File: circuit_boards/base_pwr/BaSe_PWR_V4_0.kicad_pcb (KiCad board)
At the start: 2 copper layers, 15 parts, among them J1 USB_B, J2 MOTOR, J3 MEAS, J5 Conn_02x19_Odd_Even, U1 DRV8220, U2 STM32F070CBTx

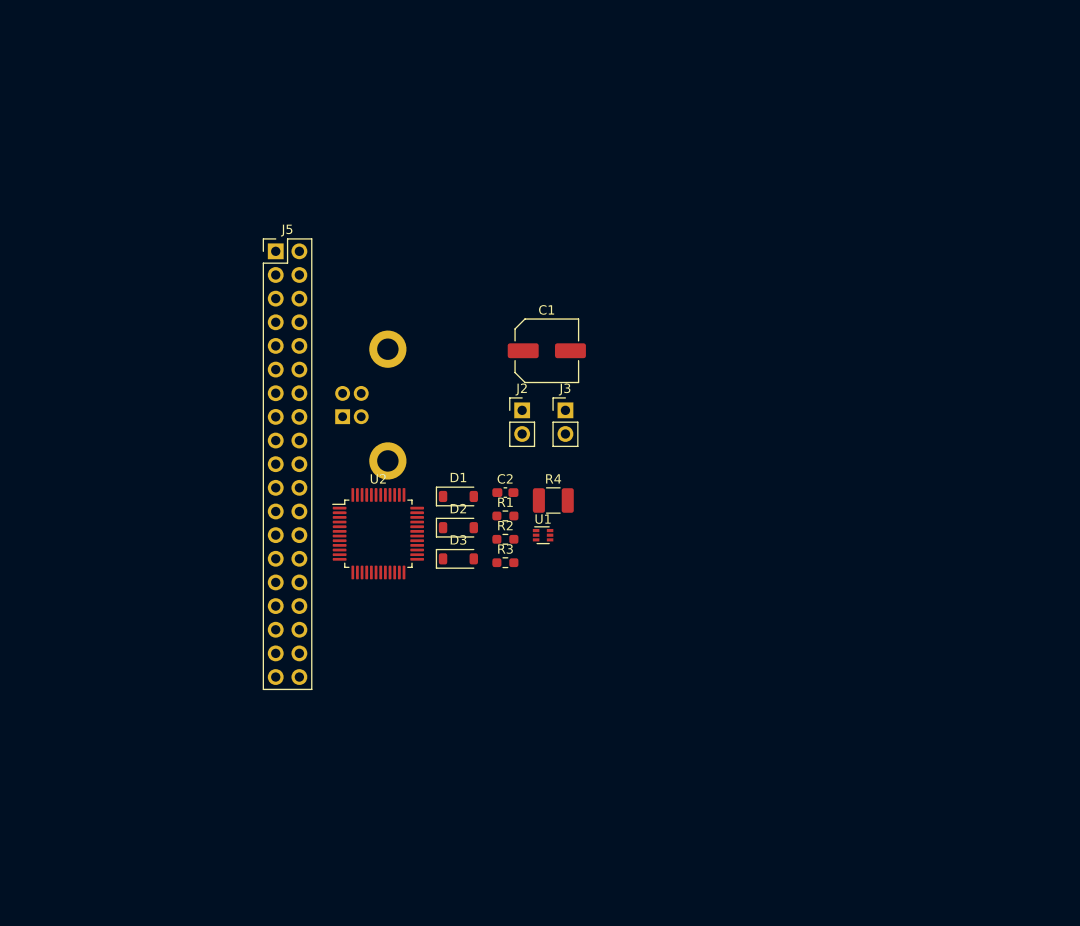
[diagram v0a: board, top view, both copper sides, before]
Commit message: base_pwr: rescure schematic parts from old version (v3.2) and start with mcu wiring
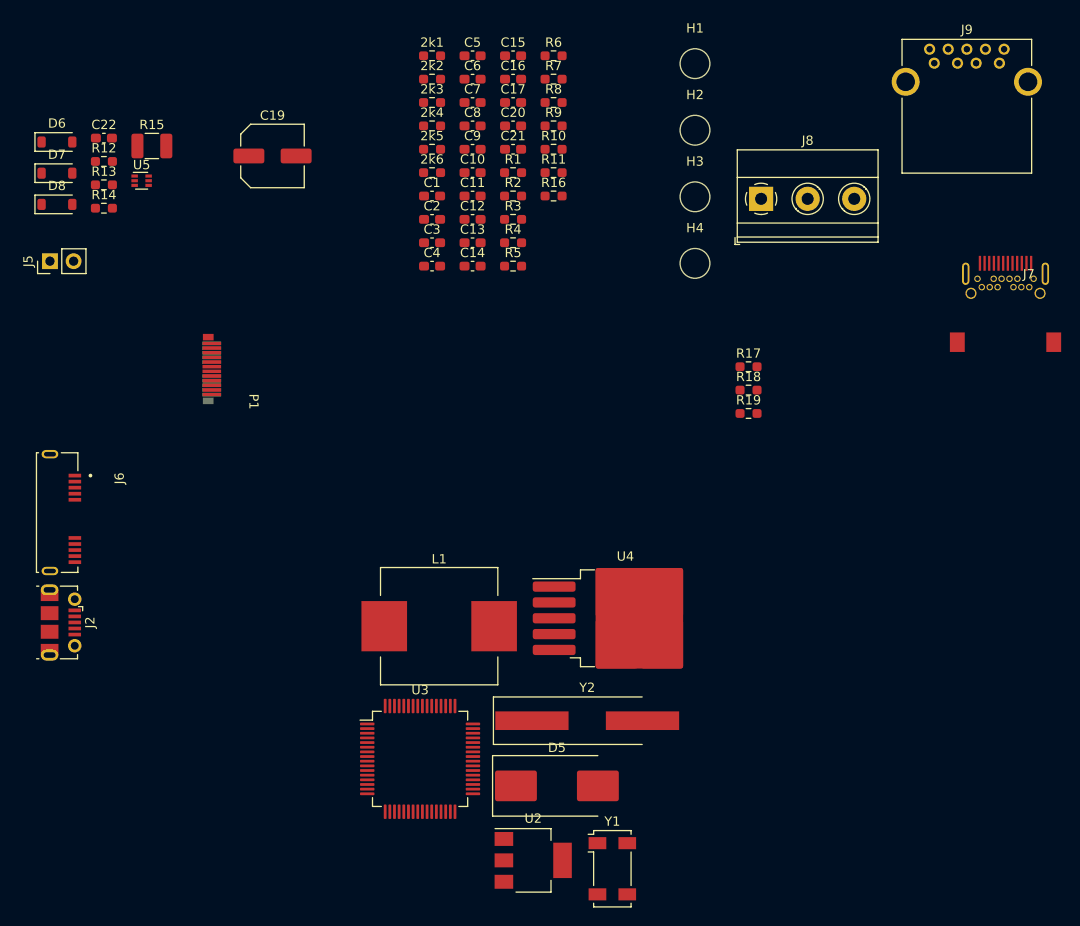
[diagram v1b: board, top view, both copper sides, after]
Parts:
- removed J1: USB_B, Connector_USB:USB_B_Lumberg_2411_02_Horizontal
- removed J3: MEAS, Connector_PinHeader_2.54mm:PinHeader_1x02_P2.54mm_Vertical
- removed the J5 at (79.2, 43.9)
- added 2k1: ~, Resistor_SMD:R_0603_1608Metric_Pad0.98x0.95mm_HandSolder, F.Cu at (96.0, 22.9)
- added 2k2: ~, Resistor_SMD:R_0603_1608Metric_Pad0.98x0.95mm_HandSolder, F.Cu at (96.0, 25.4)
- added 2k3: ~, Resistor_SMD:R_0603_1608Metric_Pad0.98x0.95mm_HandSolder, F.Cu at (96.0, 28.0)
- added 2k4: ~, Resistor_SMD:R_0603_1608Metric_Pad0.98x0.95mm_HandSolder, F.Cu at (96.0, 30.5)
- added 2k5: ~, Resistor_SMD:R_0603_1608Metric_Pad0.98x0.95mm_HandSolder, F.Cu at (96.0, 33.0)
- added 2k6: ~, Resistor_SMD:R_0603_1608Metric_Pad0.98x0.95mm_HandSolder, F.Cu at (96.0, 35.5)
- added C1: ~, Capacitor_SMD:C_0603_1608Metric_Pad1.08x0.95mm_HandSolder, F.Cu at (96.0, 38.0)
- added C10: C, Capacitor_SMD:C_0603_1608Metric_Pad1.08x0.95mm_HandSolder, F.Cu at (100.4, 35.5)
- added C11: 100nF, Capacitor_SMD:C_0603_1608Metric_Pad1.08x0.95mm_HandSolder, F.Cu at (100.4, 38.0)
- added C12: 100nF, Capacitor_SMD:C_0603_1608Metric_Pad1.08x0.95mm_HandSolder, F.Cu at (100.4, 40.5)
- added C13: 100nF, Capacitor_SMD:C_0603_1608Metric_Pad1.08x0.95mm_HandSolder, F.Cu at (100.4, 43.0)
- added C14: ~, Capacitor_SMD:C_0603_1608Metric_Pad1.08x0.95mm_HandSolder, F.Cu at (100.4, 45.5)
- added C15: 100nF, Capacitor_SMD:C_0603_1608Metric_Pad1.08x0.95mm_HandSolder, F.Cu at (104.7, 22.9)
- added C16: 100nF, Capacitor_SMD:C_0603_1608Metric_Pad1.08x0.95mm_HandSolder, F.Cu at (104.7, 25.4)
- added C17: ~, Capacitor_SMD:C_0603_1608Metric_Pad1.08x0.95mm_HandSolder, F.Cu at (104.7, 28.0)
- added C2: ~, Capacitor_SMD:C_0603_1608Metric_Pad1.08x0.95mm_HandSolder, F.Cu at (96.0, 40.5)
- added C20: ~, Capacitor_SMD:C_0603_1608Metric_Pad1.08x0.95mm_HandSolder, F.Cu at (104.7, 30.5)
- added C21: ~, Capacitor_SMD:C_0603_1608Metric_Pad1.08x0.95mm_HandSolder, F.Cu at (104.7, 33.0)
- added C3: ~, Capacitor_SMD:C_0603_1608Metric_Pad1.08x0.95mm_HandSolder, F.Cu at (96.0, 43.0)
- added C4: ~, Capacitor_SMD:C_0603_1608Metric_Pad1.08x0.95mm_HandSolder, F.Cu at (96.0, 45.5)
- added C5: 20pF, Capacitor_SMD:C_0603_1608Metric_Pad1.08x0.95mm_HandSolder, F.Cu at (100.4, 22.9)
- added C6: 20pF, Capacitor_SMD:C_0603_1608Metric_Pad1.08x0.95mm_HandSolder, F.Cu at (100.4, 25.4)
- added C7: 4.3pF, Capacitor_SMD:C_0603_1608Metric_Pad1.08x0.95mm_HandSolder, F.Cu at (100.4, 28.0)
- added C8: 4.3pF, Capacitor_SMD:C_0603_1608Metric_Pad1.08x0.95mm_HandSolder, F.Cu at (100.4, 30.5)
- added C9: 100nF, Capacitor_SMD:C_0603_1608Metric_Pad1.08x0.95mm_HandSolder, F.Cu at (100.4, 33.0)
- added D5: SK34-TP, Diode_SMD:D_SMC_Handsoldering, F.Cu at (109.4, 101.3)
- added H1: MountingHole, MountingHole:MountingHole_3.2mm_M3_DIN965, F.Cu at (124.3, 23.8)
- added H2: MountingHole, MountingHole:MountingHole_3.2mm_M3_DIN965, F.Cu at (124.3, 30.9)
- added H3: MountingHole, MountingHole:MountingHole_3.2mm_M3_DIN965, F.Cu at (124.3, 38.1)
- added H4: MountingHole, MountingHole:MountingHole_3.2mm_M3_DIN965, F.Cu at (124.3, 45.2)
- added J2: USB_B_Micro, Connector_USB:USB_Micro-B_Molex-105017-0001, F.Cu at (56.2, 83.8)
- added J6: USB3_B_Micro, g7_connectors:conn_usb3bmicro_GSB343K331HR, F.Cu at (55.0, 72.0)
- added J7: USB_C_Receptacle, g7_connectors:conn_usbc_socket_RAHPCUC31AU1TR, F.Cu at (157.6, 46.9)
- added J8: Screw_Terminal_01x03, TerminalBlock_Phoenix:TerminalBlock_Phoenix_MKDS-1,5-3_1x03_P5.00mm_Horizontal, F.Cu at (131.4, 38.3)
- added J9: USB3_A, g7_connectors:STEWARD_USB3_A_SS-52000-001, F.Cu at (153.5, 22.2)
- added L1: 47µH, Inductor_SMD:L_Wuerth_WE-PD-Typ-LS_Handsoldering, F.Cu at (96.8, 84.2)
- added P1: USB_C_Plug, g7_connectors:Molex_USBC_Plug_1054440011, F.Cu at (72.9, 56.6)
- added R1: ~, Resistor_SMD:R_0603_1608Metric_Pad0.98x0.95mm_HandSolder, F.Cu at (104.7, 35.5)
- added R10: R, Resistor_SMD:R_0603_1608Metric_Pad0.98x0.95mm_HandSolder, F.Cu at (109.1, 33.0)
- added R11: ~, Resistor_SMD:R_0603_1608Metric_Pad0.98x0.95mm_HandSolder, F.Cu at (109.1, 35.5)
- added R16: R, Resistor_SMD:R_0603_1608Metric_Pad0.98x0.95mm_HandSolder, F.Cu at (109.1, 38.0)
- added R17: 31k6, Resistor_SMD:R_0603_1608Metric_Pad0.98x0.95mm_HandSolder, F.Cu at (130.0, 56.3)
- added R18: 10k, Resistor_SMD:R_0603_1608Metric_Pad0.98x0.95mm_HandSolder, F.Cu at (130.0, 58.8)
- added R19: 38k3, Resistor_SMD:R_0603_1608Metric_Pad0.98x0.95mm_HandSolder, F.Cu at (130.0, 61.4)
- added R2: ~, Resistor_SMD:R_0603_1608Metric_Pad0.98x0.95mm_HandSolder, F.Cu at (104.7, 38.0)
- added R3: R, Resistor_SMD:R_0603_1608Metric_Pad0.98x0.95mm_HandSolder, F.Cu at (104.7, 40.5)
- added R4: R, Resistor_SMD:R_0603_1608Metric_Pad0.98x0.95mm_HandSolder, F.Cu at (104.7, 43.0)
- added R5: 100k, Resistor_SMD:R_0603_1608Metric_Pad0.98x0.95mm_HandSolder, F.Cu at (104.7, 45.5)
- added R6: 33k, Resistor_SMD:R_0603_1608Metric_Pad0.98x0.95mm_HandSolder, F.Cu at (109.1, 22.9)
- added R7: 10k, Resistor_SMD:R_0603_1608Metric_Pad0.98x0.95mm_HandSolder, F.Cu at (109.1, 25.4)
- added R8: 10k, Resistor_SMD:R_0603_1608Metric_Pad0.98x0.95mm_HandSolder, F.Cu at (109.1, 28.0)
- added R9: 47k, Resistor_SMD:R_0603_1608Metric_Pad0.98x0.95mm_HandSolder, F.Cu at (109.1, 30.5)
- added U3: STM32F070RBTx, Package_QFP:LQFP-64_10x10mm_P0.5mm, F.Cu at (94.8, 98.5)
- added U4: LM2596S-5, Package_TO_SOT_SMD:TO-263-5_TabPin3, F.Cu at (116.8, 83.3)
- added Y1: 32.768kHz, Crystal:Crystal_SMD_Abracon_ABS25-4Pin_8.0x3.8mm, F.Cu at (115.4, 110.2)
- added Y2: 8MHz, Crystal:Crystal_SMD_HC49-SD_HandSoldering, F.Cu at (112.7, 94.3)
- U2: value STM32F070CBTx -> AMS1117-3.3; footprint Package_QFP:LQFP-48_7x7mm_P0.5mm -> Package_TO_SOT_SMD:SOT-223-3_TabPin2
- moved D7 57.5 mm to (55.8, 35.5)
- moved R13 57.5 mm to (60.8, 36.8)
- moved U5 57.5 mm to (64.8, 36.4)
- moved C22 57.5 mm to (60.8, 31.8)
- moved D6 57.5 mm to (55.8, 32.2)
- moved D8 57.5 mm to (55.8, 38.9)
- moved R12 57.5 mm to (60.8, 34.3)
- moved R14 57.5 mm to (60.8, 39.3)
- moved R15 57.5 mm to (65.9, 32.6)
- moved J5 53.2 mm to (55.0, 45.0), turned to 90 degrees
- moved U2 38.8 mm to (106.9, 109.3)
- moved C19 36.1 mm to (78.9, 33.7)
- renumbered C1 to C19, C2 to C22, D1 to D6, D2 to D7, D3 to D8, J2 to J5, R1 to R12, R2 to R13, R3 to R14, R4 to R15, U1 to U5
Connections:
- C19 pad 1: Vdrive -> +12V
- C22 pad 1: Vdrive -> +12V
- U2 pad 1: unconnected-(U2-VDD-Pad1) -> GND
- U2 pad 2: unconnected-(U2-PC13-Pad2) -> +3V3_STBY
- U2 pad 3: unconnected-(U2-PC14-Pad3) -> +12V
- U5 pad 5: Vdrive -> +12V

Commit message: BaSe_PWR_V4_0: wire up things
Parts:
- removed 2k2, R11: ~, Resistor_SMD:R_0603_1608Metric_Pad0.98x0.95mm_HandSolder
- removed H1, H2: MountingHole, MountingHole:MountingHole_3.2mm_M3_DIN965
- removed R16: R, Resistor_SMD:R_0603_1608Metric_Pad0.98x0.95mm_HandSolder
- added 2k10: ~, Resistor_SMD:R_0603_1608Metric_Pad0.98x0.95mm_HandSolder, F.Cu at (136.2, 96.8)
- added 2k7: ~, Resistor_SMD:R_0603_1608Metric_Pad0.98x0.95mm_HandSolder, F.Cu at (136.2, 89.2)
- added 2k8: ~, Resistor_SMD:R_0603_1608Metric_Pad0.98x0.95mm_HandSolder, F.Cu at (136.2, 91.8)
- added 2k9: ~, Resistor_SMD:R_0603_1608Metric_Pad0.98x0.95mm_HandSolder, F.Cu at (136.2, 94.3)
- added C23: 100nF, Capacitor_SMD:C_0603_1608Metric_Pad1.08x0.95mm_HandSolder, F.Cu at (140.5, 89.2)
- added C25: 10nF, Capacitor_SMD:C_0603_1608Metric_Pad1.08x0.95mm_HandSolder, F.Cu at (140.5, 91.8)
- added C26: 1µF, Capacitor_SMD:C_0603_1608Metric_Pad1.08x0.95mm_HandSolder, F.Cu at (140.5, 94.3)
- added C27: C, Capacitor_SMD:C_0603_1608Metric_Pad1.08x0.95mm_HandSolder, F.Cu at (140.5, 96.8)
- added C28: 100nF, Capacitor_SMD:C_0603_1608Metric_Pad1.08x0.95mm_HandSolder, F.Cu at (140.5, 99.3)
- added C30: ~, Capacitor_SMD:C_0603_1608Metric_Pad1.08x0.95mm_HandSolder, F.Cu at (144.9, 89.2)
- added C31: ~, Capacitor_SMD:C_0603_1608Metric_Pad1.08x0.95mm_HandSolder, F.Cu at (144.9, 91.8)
- added D10: ~, Diode_SMD:D_SOD-123F, F.Cu at (213.0, 22.0)
- added D12: ~, Diode_SMD:D_SOD-123F, F.Cu at (213.0, 25.4)
- added D13: ~, Diode_SMD:D_SOD-123F, F.Cu at (213.0, 28.7)
- added D9: ~, Diode_SMD:D_SOD-123F, F.Cu at (207.5, 28.2)
- added FL1: ~, g7_emi:CMC_Laird_CM2021Y330R-10, F.Cu at (188.2, 33.3)
- added FL2: ~, g7_emi:CMC_Laird_CM2021Y330R-10, F.Cu at (188.2, 39.5)
- added FL3: ~, g7_emi:CMC_Laird_CM2021Y330R-10, F.Cu at (188.2, 45.7)
- added J4: Screw_Terminal_01x04, TerminalBlock_Phoenix:TerminalBlock_Phoenix_MKDS-1,5-4_1x04_P5.00mm_Horizontal, F.Cu at (186.7, 24.6)
- added K1: ~, g7_relay:Kemet_EC2-12TNU, F.Cu at (195.3, 32.3)
- added K2: ~, g7_relay:Kemet_EC2-12TNU, F.Cu at (204.5, 32.3)
- added Q2: BSS214NW, Package_TO_SOT_SMD:SOT-323_SC-70, F.Cu at (216.9, 32.5)
- added Q3: BSS214NW, Package_TO_SOT_SMD:SOT-323_SC-70, F.Cu at (216.9, 36.1)
- added Q4: BSS214NW, Package_TO_SOT_SMD:SOT-323_SC-70, F.Cu at (216.9, 39.8)
- added Q5: BSS214NW, Package_TO_SOT_SMD:SOT-323_SC-70, F.Cu at (216.9, 43.4)
- added U6: AMS1117-3.3, Package_TO_SOT_SMD:SOT-223-3_TabPin2, F.Cu at (138.9, 104.7)
- moved R6 82.1 mm to (144.9, 96.8)
- moved C11 71.0 mm to (136.2, 99.3)
- moved R5 63.1 mm to (144.9, 94.3)
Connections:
- net /adc_vbat renamed /12vin_meas
- net /hmi_miso2_sda2 renamed /Dis_DB6
- net /hmi_mosi2 renamed /Dis_DB7
- net /hmi_nss2 renamed /Dis_DB4
- net /hmi_pushbutton_1 renamed /spi1_sck
- net /hmi_pwm0 renamed /Dis_PWM
- net /hmi_sck2_scl2 renamed /Dis_DB5
- net /hmi_usart_rx3 renamed /Dis_E
- net /hmi_usart_tx3 renamed /Dis_RS
- 2k1 pad 1: /LED_HMI_attiny -> /hmi_pwm1
- 2k3 pad 1: /SW_HDD_On -> /sw_sbu_on
- 2k6 pad 1: /SW_HDD_Off -> /sw_sbu_off
- C20 pad 1: Net-(C20-Pad1) -> /+5V_sbu
- C21 pad 1: Net-(J4-Pin_2) -> /+5v_sbu_flt
- C21 pad 2: Net-(J4-Pin_1) -> /+5v_sbu_flt_gnd
- R5 pad 2: +12V -> /12V_nProt
- U3 pad 10: unconnected-(U3-PC2-Pad10) -> /sw_sbu_on
- U3 pad 11: unconnected-(U3-PC3-Pad11) -> /sw_sbu_off
- U3 pad 12: unconnected-(U3-VSSA-Pad12) -> GND
- U3 pad 13: +3V3_STBY -> +3.3VA
- U3 pad 16: unconnected-(U3-PA2-Pad16) -> /usart2_tx
- U3 pad 17: unconnected-(U3-PA3-Pad17) -> /usart2_rx
- U3 pad 18: Net-(U3-VSS-Pad18) -> GND
- U3 pad 23: unconnected-(U3-PA7-Pad23) -> /in2_mcu
- U3 pad 24: unconnected-(U3-PC4-Pad24) -> /~{LM2596S_ON}
- U3 pad 25: unconnected-(U3-PC5-Pad25) -> /Taster_0
- U3 pad 28: /hmi_pushbutton_0 -> unconnected-(U3-PB2-Pad28)
- U3 pad 31: Net-(U3-VSS-Pad18) -> GND
- U3 pad 37: unconnected-(U3-PC6-Pad37) -> /Taster_1
- U3 pad 41: unconnected-(U3-PA8-Pad41) -> /in1_mcu
- U3 pad 46: unconnected-(U3-PA13-Pad46) -> /swdio
- U3 pad 47: Net-(U3-VSS-Pad18) -> GND
- U3 pad 49: unconnected-(U3-PA14-Pad49) -> /swclk
- U3 pad 50: unconnected-(U3-PA15-Pad50) -> /spi1_nss
- U3 pad 56: unconnected-(U3-PB4-Pad56) -> /spi1_cipo
- U3 pad 57: unconnected-(U3-PB5-Pad57) -> /spi1_copi
- U3 pad 58: unconnected-(U3-PB6-Pad58) -> /usart1_tx
- U3 pad 59: unconnected-(U3-PB7-Pad59) -> /usart1_rx
- U3 pad 61: unconnected-(U3-PB8-Pad61) -> /i2c1_scl
- U3 pad 62: unconnected-(U3-PB9-Pad62) -> /i2c1_sda
- U3 pad 63: Net-(U3-VSS-Pad18) -> GND
- U3 pad 8: unconnected-(U3-PC0-Pad8) -> /SW_HDD_On
- U3 pad 9: unconnected-(U3-PC1-Pad9) -> /SW_HDD_Off
